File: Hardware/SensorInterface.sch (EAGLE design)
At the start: 49 parts, among them J3 CONN_3SCREW_254, J4 CONN_42.54_SCREW, Q1 DMG3404, Q2 2N7002, Q3 2N7002, Q4 DMG3404, Q5 DMG3404, U10 SN74AHC1G86DCK, U11 MCP6041, U12 MCP4725A1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

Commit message: Edits to schematic and simulations
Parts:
- U$3: value ATTINY441/841841 -> ATTINY441/841841SOIC; device bschulz:ATTINY441/841841 -> bschulz:ATTINY441/841841SOIC
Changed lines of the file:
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@@
 <part name="Q1" library="bschulz" deviceset="MOSFET-NCH" device="-DMG3404L" value="DMG3404"/>
 <part name="GND3" library="supply1" library_urn="urn:adsk.eagle:library:371" deviceset="GND" device=""/>
-<part name="U$3" library="bschulz" deviceset="ATTINY441/841" device="" technology="841"/>
+<part name="U$3" library="bschulz" deviceset="ATTINY441/841" device="SOIC" technology="841" value="ATTINY441/841841SOIC"/>
 <part name="ISP1" library="bschulz" deviceset="AVRISP" device="-6"/>
 <part name="C3" library="bschulz_passives" deviceset="C-EU" device="C0603" value="0.1uF"/>

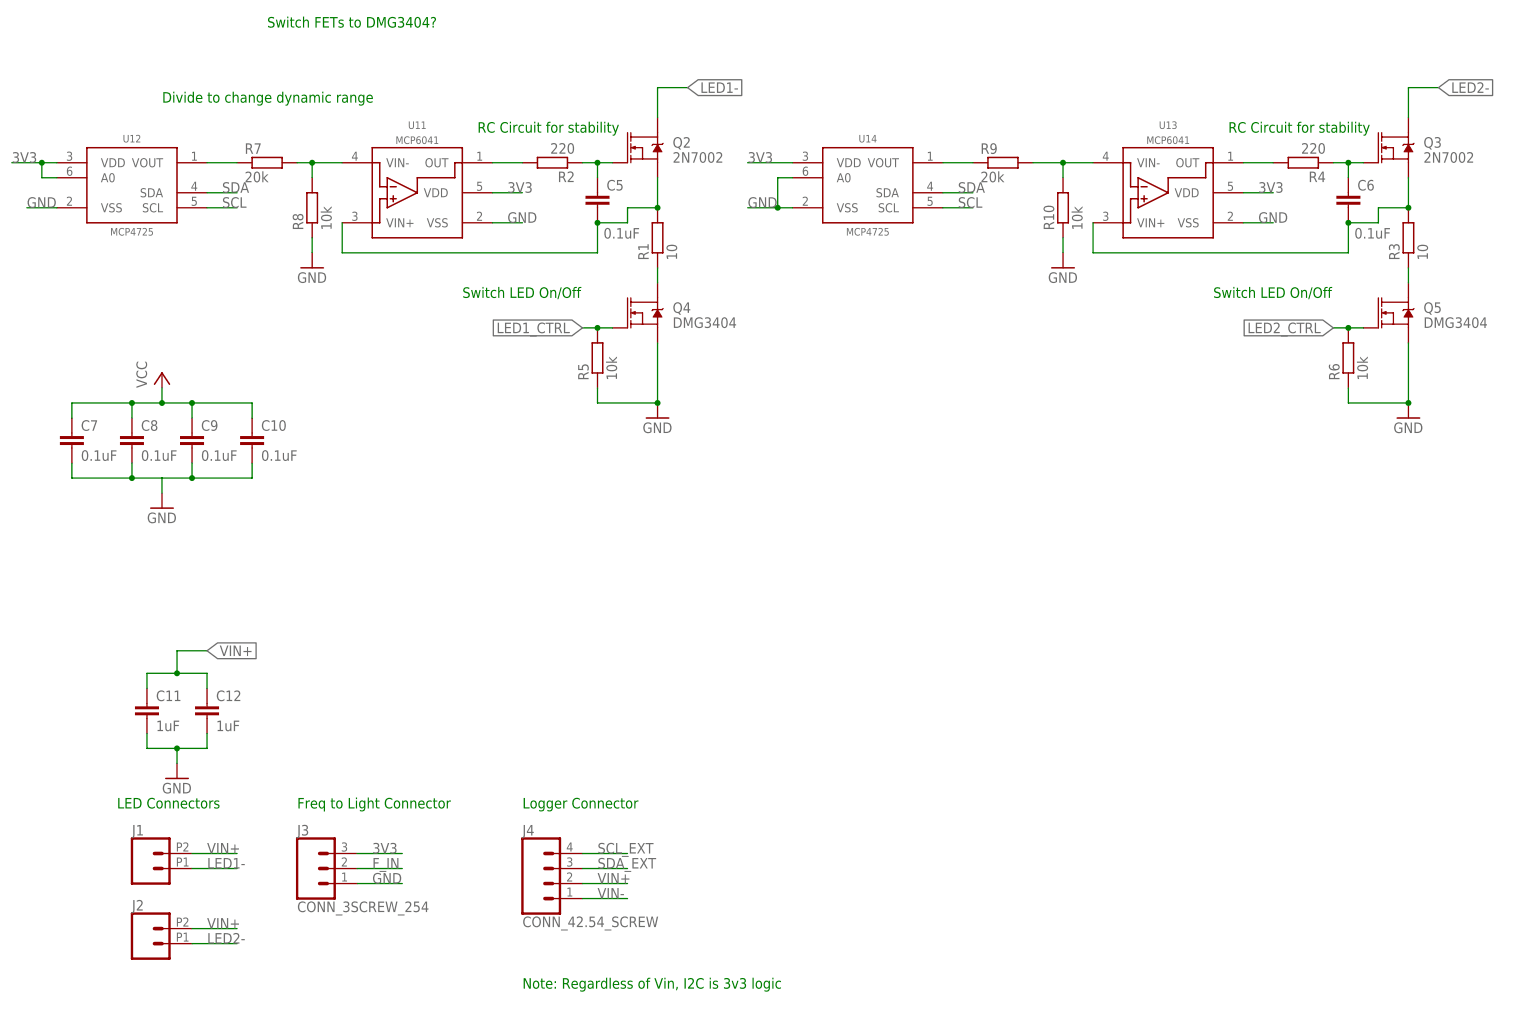
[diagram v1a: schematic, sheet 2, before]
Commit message: +1 detector, MUX, 3V3 labels
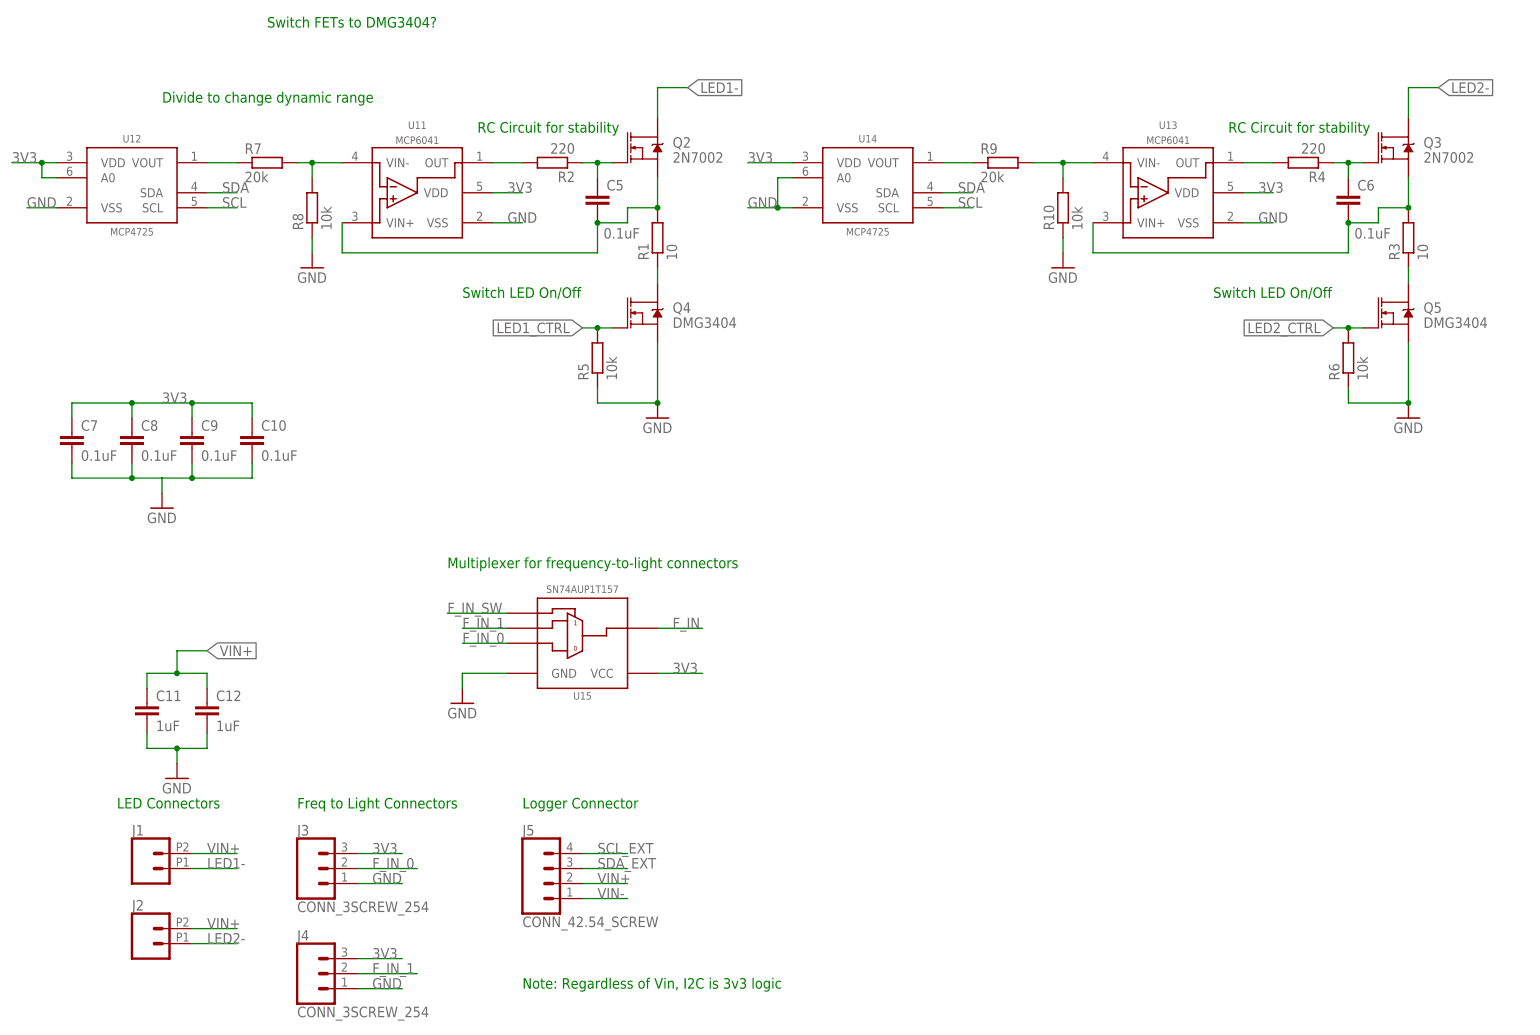
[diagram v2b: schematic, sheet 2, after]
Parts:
- added J5: CONN_42.54_SCREW, bschulz:CONN_42.54_SCREW
- added U15: SN74AUP1T157DCK, bschulz:SN74AUP1T157DCK
- J4: value CONN_42.54_SCREW -> CONN_3SCREW_254; device bschulz:CONN_42.54_SCREW -> bschulz:CONN_3SCREW_254
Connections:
- new net F_IN_0: J3.2, U15.B
- new net F_IN_1: J4.2, U15.A
- new net F_IN_SW: U$3.PA2, U15.C
- net 3V3: now also J4.3, U15.VCC
- net F_IN: now also U15.Y; no longer J3.2
- net GND: now also J4.1, U15.GND
- net SCL_EXT: now also J5.4; no longer J4.4
- net SDA_EXT: now also J5.3; no longer J4.3
- net VIN+: now also J5.2; no longer J4.2
- net VIN-: now also J5.1; no longer J4.1
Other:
- note added: "Freq to Light Connectors"
- note added: "Multiplexer for frequency-to-light connectors"
- note removed: "Freq to Light Connector"

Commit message: Silkscreen for initial prototype
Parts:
- added LOGO1: OSHW-LOGOM, SparkFun-Aesthetics:OSHW-LOGOM
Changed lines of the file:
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@@
 <part name="U15" library="bschulz" deviceset="SN74AUP1T157" device="DCK"/>
 <part name="GND11" library="supply1" library_urn="urn:adsk.eagle:library:371" deviceset="GND" device=""/>
+<part name="LOGO1" library="SparkFun-Aesthetics" deviceset="OSHW-LOGO" device="M"/>
 </parts>
 <sheets>
@@
 <attribute name="VALUE" x="81.28" y="83.82" size="1.778" layer="96"/>
 </instance>
+<instance part="LOGO1" gate="G$1" x="193.04" y="93.98"/>
 </instances>
 <busses>

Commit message: Post-review update * Shortened analog feedback and power traces * Checked trace widths for uniformity and appropriateness * Added 5V/3.3V level conversion * Pull-ups on I2C (internal) and RESET
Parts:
- added C13, C14: 0.1uF, bschulz_passives:C-EUC0603
- added R11, R12, R13: 10k, bschulz_passives:R-EU_R0603
- added U16: TXS0102DQM, bschulz:TXS0102DQM
- R3: value 10 -> 10k
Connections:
- net !RESET: now also R13.1
- net 3V3: now also C13.1, R11.2, R12.2, R13.2, U16.EN, U16.VA
- net GND: now also C13.2, C14.2, U16.GND
- net SCL: now also R11.1, U16.A1
- net SCL_EXT: now also U16.B1
- net SDA: now also R12.1, U16.A2
- net SDA_EXT: now also U16.B2
- net VIN+: now also C14.1, U16.VB
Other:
- note added: "Communications: I2C"

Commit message: Added gerbers, minor cleanup, v0.0.0 submitted to fab
Cleaned up board and made some minor changes to decoupling capacitor layout, adjusted some traces. Generated gerbers and submitted boards for v0.0
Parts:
- removed C12: 1uF, bschulz_passives:C-EUC0603
- J3, J4: value CONN_3SCREW_254 -> CONN_32.54_SCREW; device bschulz:CONN_3SCREW_254 -> bschulz:CONN_32.54_SCREW
- renumbered JP1 to JP0
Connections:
- net GND: no longer C12.2
- net VIN+: no longer C12.1

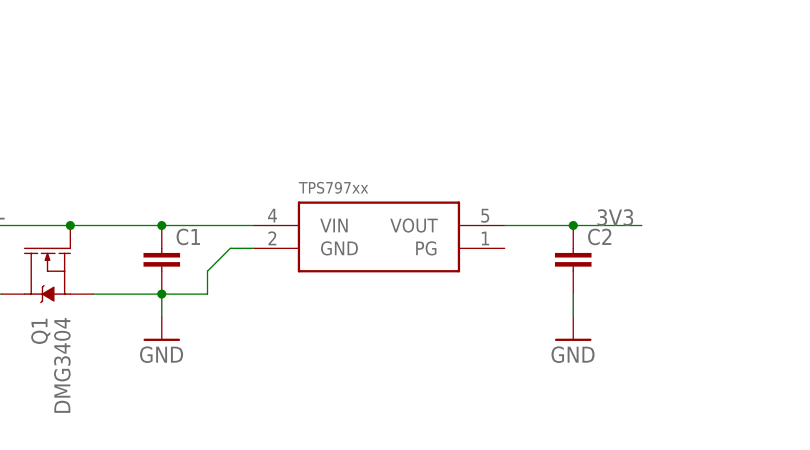
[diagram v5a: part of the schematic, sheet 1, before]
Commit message: Move and define caps
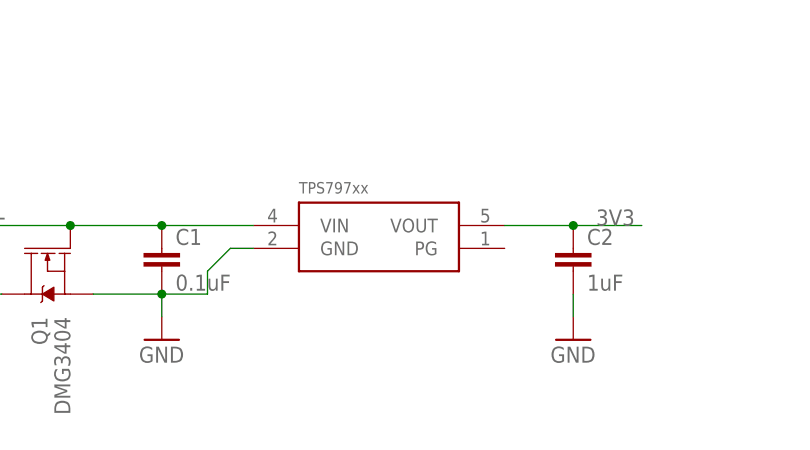
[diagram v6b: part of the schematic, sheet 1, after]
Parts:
- C1: value (none) -> 0.1uF; device bschulz_passives:C-EUC0603 -> bschulz_passives:C-EU0.1UFC0603
- C2: value (none) -> 1uF; device bschulz_passives:C-EUC0603 -> bschulz_passives:C-EU1UFC0603
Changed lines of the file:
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@@
 <?xml version="1.0" encoding="utf-8"?>
 <!DOCTYPE eagle SYSTEM "eagle.dtd">
-<eagle version="9.2.1">
+<eagle version="9.2.2">
 <drawing>
 <settings>
@@
 <setting verticaltext="up"/>
 </settings>
-<grid distance="0.1" unitdist="inch" unit="mm" style="lines" multiple="1" display="no" altdistance="0.01" altunitdist="inch" altunit="mm"/>
+<grid distance="0.1" unitdist="inch" unit="inch" style="lines" multiple="1" display="no" altdistance="0.01" altunitdist="inch" altunit="inch"/>
 <layers>
-<layer number="1" name="Top" color="4" fill="1" visible="no" active="no"/>
-<layer number="2" name="Route2" color="1" fill="3" visible="no" active="no"/>
-<layer number="3" name="Route3" color="4" fill="3" visible="no" active="no"/>
-<layer number="4" name="Route4" color="1" fill="4" visible="no" active="no"/>
-<layer number="5" name="Route5" color="4" fill="4" visible="no" active="no"/>
-<layer number="6" name="Route6" color="1" fill="8" visible="no" active="no"/>
-<layer number="7" name="Route7" color="4" fill="8" visible="no" active="no"/>
-<layer number="8" name="Route8" color="1" fill="2" visible="no" active="no"/>
-<layer number="9" name="Route9" color="4" fill="2" visible="no" active="no"/>
-<layer number="10" name="Route10" color="1" fill="7" visible="no" active="no"/>
-<layer number="11" name="Route11" color="4" fill="7" visible="no" active="no"/>
-<layer number="12" name="Route12" color="1" fill="5" visible="no" active="no"/>
-<layer number="13" name="Route13" color="4" fill="5" visible="no" active="no"/>
-<layer number="14" name="Route14" color="1" fill="6" visible="no" active="no"/>
-<layer number="15" name="Route15" color="4" fill="6" visible="no" active="no"/>
-<layer number="16" name="Bottom" color="1" fill="1" visible="no" active="no"/>
-<layer number="17" name="Pads" color="2" fill="1" visible="no" active="no"/>
-<layer number="18" name="Vias" color="2" fill="1" visible="no" active="no"/>
-<layer number="19" name="Unrouted" color="6" fill="1" visible="no" active="no"/>
-<layer number="20" name="Dimension" color="15" fill="1" visible="no" active="no"/>
-<layer number="21" name="tPlace" color="7" fill="1" visible="no" active="no"/>
-<layer number="22" name="bPlace" color="7" fill="1" visible="no" active="no"/>
-<layer number="23" name="tOrigins" color="15" fill="1" visible="no" active="no"/>
-<layer number="24" name="bOrigins" color="15" fill="1" visible="no" active="no"/>
-<layer number="25" name="tNames" color="7" fill="1" visible="no" active="no"/>
-<layer number="26" name="bNames" color="7" fill="1" visible="no" active="no"/>
-<layer number="27" name="tValues" color="7" fill="1" visible="no" active="no"/>
-<layer number="28" name="bValues" color="7" fill="1" visible="no" active="no"/>
+<layer number="1" name="Top" color="4" fill="1" visible="yes" active="no"/>
+<layer number="2" name="Route2" color="1" fill="3" visible="yes" active="no"/>
+<layer number="3" name="Route3" color="4" fill="3" visible="yes" active="no"/>
+<layer number="4" name="Route4" color="1" fill="4" visible="yes" active="no"/>
+<layer number="5" name="Route5" color="4" fill="4" visible="yes" active="no"/>
+<layer number="6" name="Route6" color="1" fill="8" visible="yes" active="no"/>
+<layer number="7" name="Route7" color="4" fill="8" visible="yes" active="no"/>
+<layer number="8" name="Route8" color="1" fill="2" visible="yes" active="no"/>
+<layer number="9" name="Route9" color="4" fill="2" visible="yes" active="no"/>
+<layer number="10" name="Route10" color="1" fill="7" visible="yes" active="no"/>
+<layer number="11" name="Route11" color="4" fill="7" visible="yes" active="no"/>
+<layer number="12" name="Route12" color="1" fill="5" visible="yes" active="no"/>
+<layer number="13" name="Route13" color="4" fill="5" visible="yes" active="no"/>
+<layer number="14" name="Route14" color="1" fill="6" visible="yes" active="no"/>
+<layer number="15" name="Route15" color="4" fill="6" visible="yes" active="no"/>
+<layer number="16" name="Bottom" color="1" fill="1" visible="yes" active="no"/>
+<layer number="17" name="Pads" color="2" fill="1" visible="yes" active="no"/>
+<layer number="18" name="Vias" color="2" fill="1" visible="yes" active="no"/>
+<layer number="19" name="Unrouted" color="6" fill="1" visible="yes" active="no"/>
+<layer number="20" name="Dimension" color="24" fill="1" visible="yes" active="no"/>
+<layer number="21" name="tPlace" color="7" fill="1" visible="yes" active="no"/>
+<layer number="22" name="bPlace" color="7" fill="1" visible="yes" active="no"/>
+<layer number="23" name="tOrigins" color="15" fill="1" visible="yes" active="no"/>
+<layer number="24" name="bOrigins" color="15" fill="1" visible="yes" active="no"/>
+<layer number="25" name="tNames" color="7" fill="1" visible="yes" active="no"/>
+<layer number="26" name="bNames" color="7" fill="1" visible="yes" active="no"/>
+<layer number="27" name="tValues" color="7" fill="1" visible="yes" active="no"/>
+<layer number="28" name="bValues" color="7" fill="1" visible="yes" active="no"/>
 <layer number="29" name="tStop" color="7" fill="3" visible="no" active="no"/>
 <layer number="30" name="bStop" color="7" fill="6" visible="no" active="no"/>
@@
 <layer number="35" name="tGlue" color="7" fill="4" visible="no" active="no"/>
 <layer number="36" name="bGlue" color="7" fill="5" visible="no" active="no"/>
-<layer number="37" name="tTest" color="7" fill="1" visible="no" active="no"/>
-<layer number="38" name="bTest" color="7" fill="1" visible="no" active="no"/>
+<layer number="37" name="tTest" color="7" fill="1" visible="yes" active="no"/>
+<layer number="38" name="bTest" color="7" fill="1" visible="yes" active="no"/>
 <layer number="39" name="tKeepout" color="4" fill="11" visible="no" active="no"/>
 <layer number="40" name="bKeepout" color="1" fill="11" visible="no" active="no"/>
@@
 <layer number="44" name="Drills" color="7" fill="1" visible="no" active="no"/>
 <layer number="45" name="Holes" color="7" fill="1" visible="no" active="no"/>
-<layer number="46" name="Milling" color="3" fill="1" visible="no" active="no"/>
-<layer number="47" name="Measures" color="7" fill="1" visible="no" active="no"/>
-<layer number="48" name="Document" color="7" fill="1" visible="no" active="no"/>
-<layer number="49" name="Reference" color="7" fill="1" visible="no" active="no"/>
-<layer number="50" name="dxf" color="7" fill="1" visible="no" active="no"/>
-<layer number="51" name="tDocu" color="7" fill="1" visible="no" active="no"/>
-<layer number="52" name="bDocu" color="7" fill="1" visible="no" active="no"/>
-<layer number="53" name="tGND_GNDA" color="7" fill="1" visible="no" active="no"/>
-<layer number="54" name="bGND_GNDA" color="7" fill="1" visible="no" active="no"/>
-<layer number="56" name="wert" color="7" fill="1" visible="no" active="no"/>
-<layer number="57" name="tCAD" color="7" fill="1" visible="no" active="no"/>
-<layer number="59" name="tCarbon" color="7" fill="1" visible="no" active="no"/>
-<layer number="60" name="bCarbon" color="7" fill="1" visible="no" active="no"/>
+<layer number="46" name="Milling" color="3" fill="1" visible="yes" active="no"/>
+<layer number="47" name="Measures" color="7" fill="1" visible="yes" active="no"/>
+<layer number="48" name="Document" color="7" fill="1" visible="yes" active="no"/>
+<layer number="49" name="Reference" color="7" fill="1" visible="yes" active="no"/>
+<layer number="50" name="dxf" color="7" fill="1" visible="yes" active="no"/>
+<layer number="51" name="tDocu" color="7" fill="1" visible="yes" active="no"/>
+<layer number="52" name="bDocu" color="7" fill="1" visible="yes" active="no"/>
+<layer number="53" name="tGND_GNDA" color="7" fill="1" visible="yes" active="no"/>
+<layer number="54" name="bGND_GNDA" color="7" fill="1" visible="yes" active="no"/>
+<layer number="56" name="wert" color="7" fill="1" visible="yes" active="no"/>
+<layer number="57" name="tCAD" color="7" fill="1" visible="yes" active="no"/>
+<layer number="59" name="tCarbon" color="7" fill="1" visible="yes" active="no"/>
+<layer number="60" name="bCarbon" color="7" fill="1" visible="yes" active="no"/>
 <layer number="88" name="SimResults" color="9" fill="1" visible="yes" active="yes"/>
 <layer number="89" name="SimProbes" color="9" fill="1" visible="yes" active="yes"/>
@@
 <part name="GND1" library="supply1" library_urn="urn:adsk.eagle:library:371" deviceset="GND" device=""/>
 <part name="U$1" library="bschulz" deviceset="TPS797*" device="" technology="33"/>
-<part name="C1" library="bschulz_passives" deviceset="C-EU" device="C0603"/>
-<part name="C2" library="bschulz_passives" deviceset="C-EU" device="C0603"/>
+<part name="C1" library="bschulz_passives" deviceset="C-EU" device="C0603" technology="0.1UF" value="0.1uF"/>
+<part name="C2" library="bschulz_passives" deviceset="C-EU" device="C0603" technology="1UF" value="1uF"/>
 <part name="GND2" library="supply1" library_urn="urn:adsk.eagle:library:371" deviceset="GND" device=""/>
 <part name="Q1" library="bschulz" deviceset="MOSFET-NCH" device="-DMG3404L" value="DMG3404"/>
